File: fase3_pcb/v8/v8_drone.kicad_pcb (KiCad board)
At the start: 6 copper layers, 162 x 144.9 mm, 319 parts, among them J1 AMASS, J2 USB, Q1 TO-252-2, SW1 SW, SW2 SW, U10 SOIC-16, U11 SOIC-16, U8 SOIC-16, U9 SOIC-16

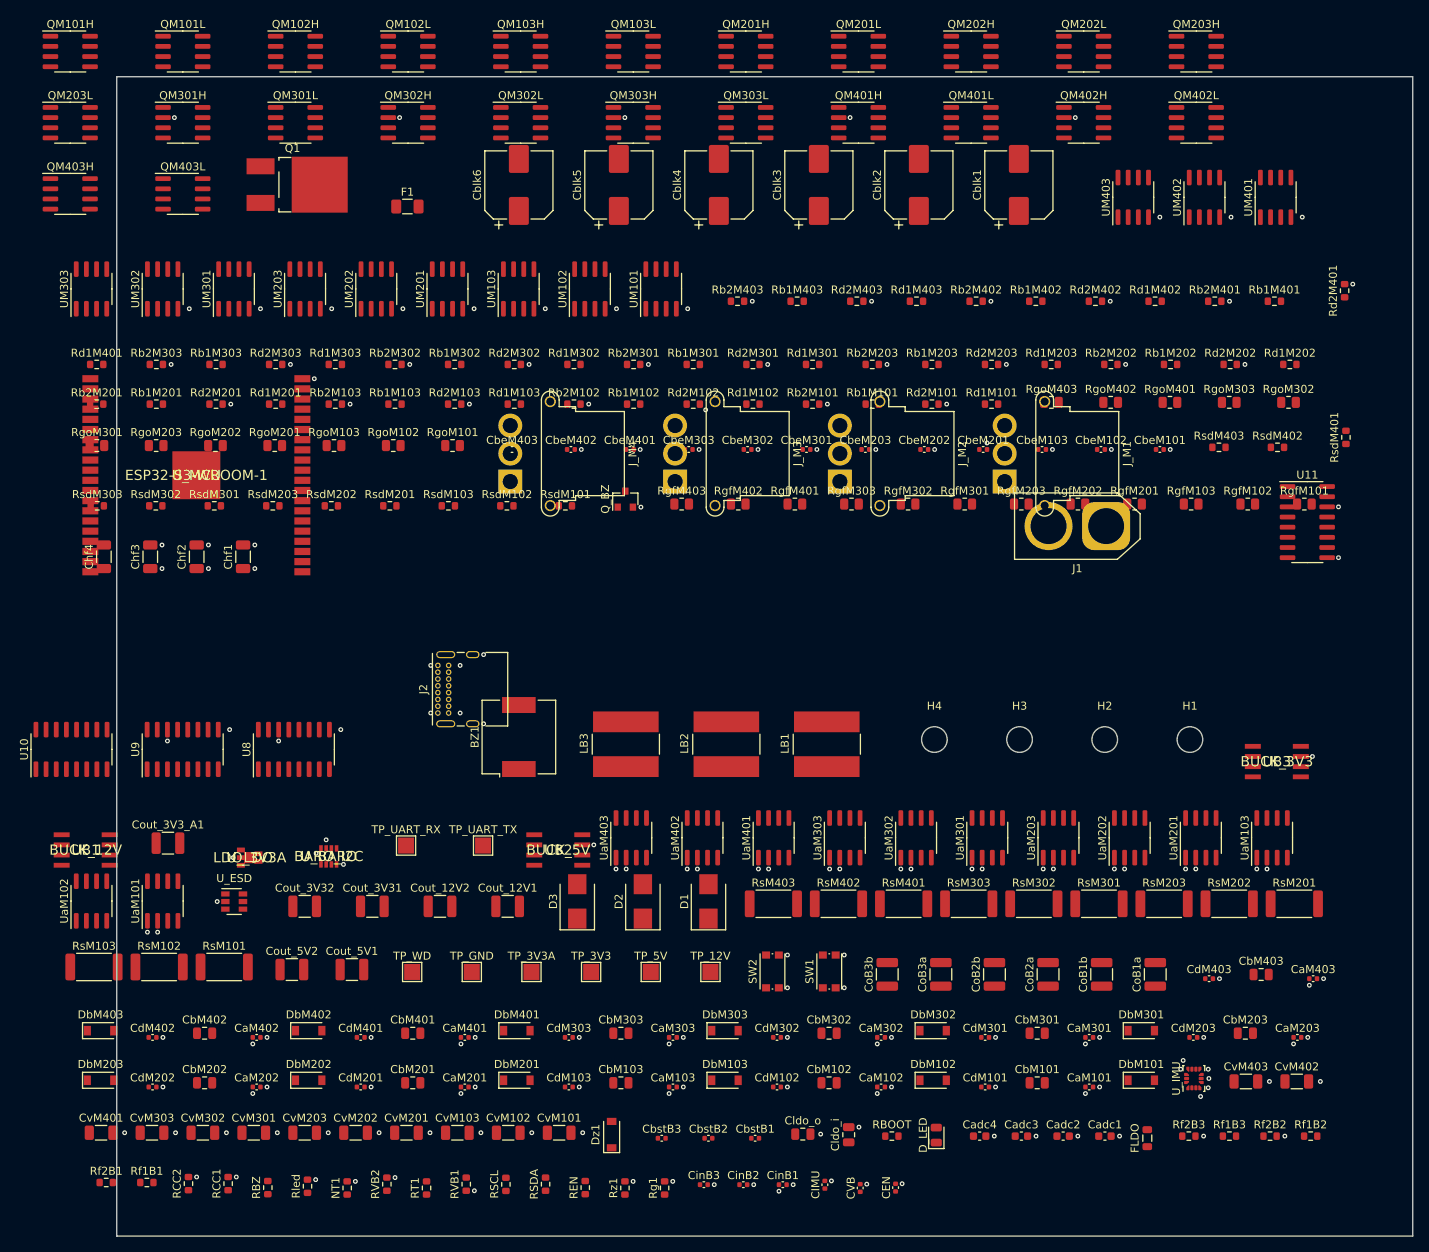
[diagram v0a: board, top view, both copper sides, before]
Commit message: feat(Fase 3): roteamento do board v8 de 6 camadas
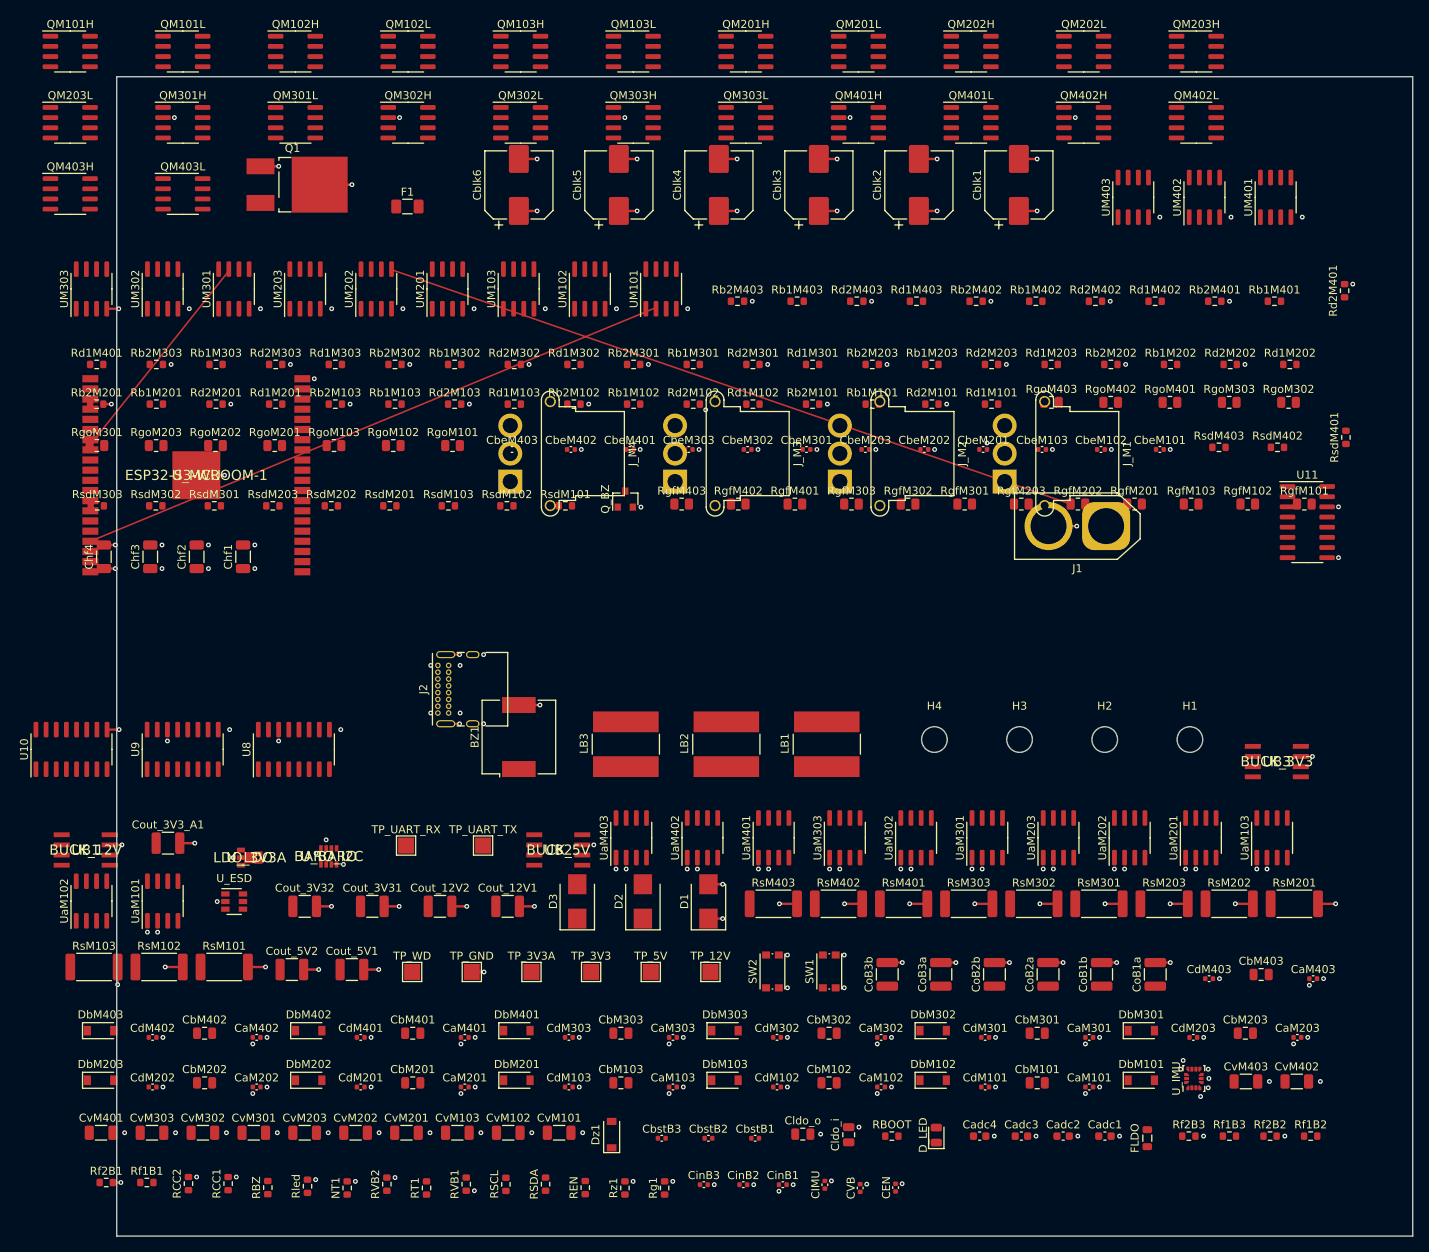
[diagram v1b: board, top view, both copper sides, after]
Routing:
- net LOM202: track 0.00 -> 89.9 mm
- net GND: track 0.00 -> 89.0 mm, vias 157 -> 201
- net PWM_M101: track 0.00 -> 76.6 mm
- net HOM301: track 0.00 -> 28.2 mm
- net VBAT_PROT: track 0.00 -> 23.2 mm, vias 23 -> 33
